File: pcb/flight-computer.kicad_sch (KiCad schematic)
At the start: 42 parts, among them J1 MicroSD Slot, J2 USB_C_Receptacle_USB2.0_16P, SW1 SW_Push, SW2 SW_Push, U1 RP2040, U2 W25Q16JVSS, U3 USBLC6-2SC6, Y1 12MHz

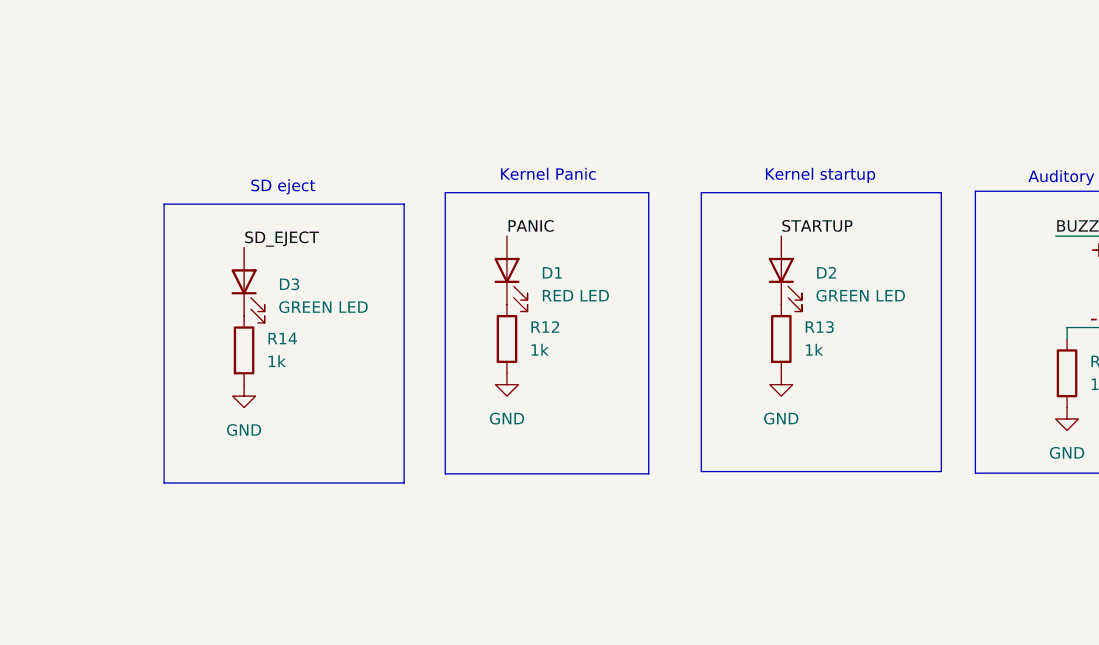
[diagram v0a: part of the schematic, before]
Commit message: Filled out the BOM for the schematic. Consolidated some components and changed footprint sizes.
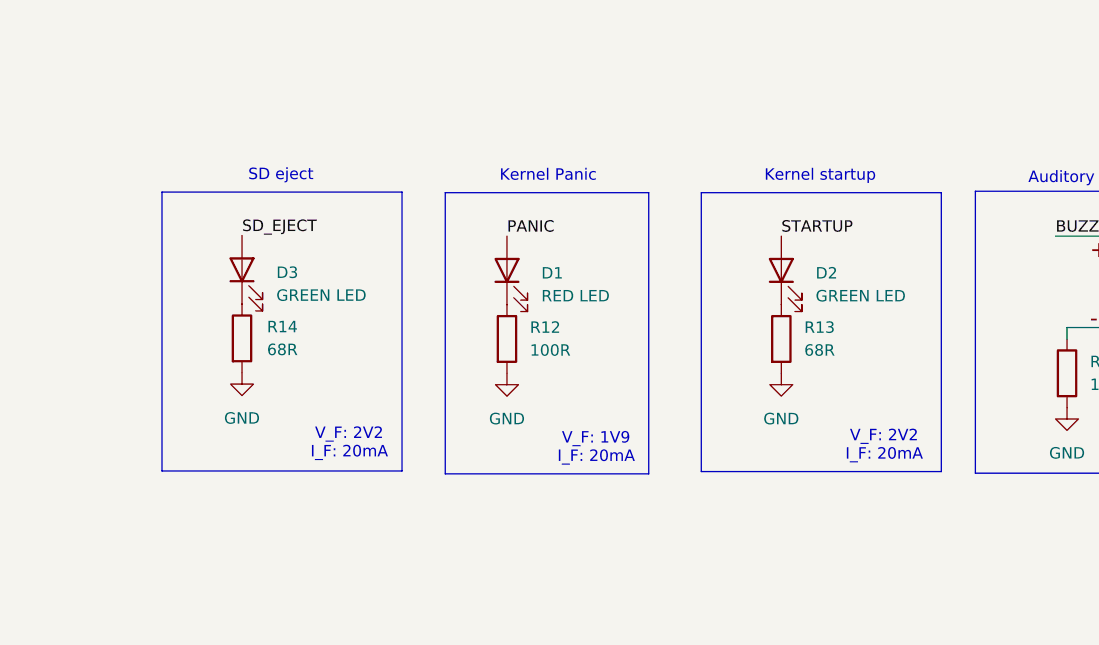
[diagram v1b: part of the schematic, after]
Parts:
- C1, C2: MP (none) -> 04023U140GAT2A
- C10, C11, C12, C13, C14, C15, C3, C5, C6, C8, C9: footprint Capacitor_SMD:C_0201_0603Metric -> Capacitor_SMD:C_0402_1005Metric; MP (none) -> GRM155R61A104KA01J
- C4: MP (none) -> GRM155C80J225KE95J
- C7: MP (none) -> 06036C105MAT2A
- D1: MP (none) -> HSMC-C170-T0000
- D2, D3: MP (none) -> LG R971-KN-1
- J1: MP (none) -> MEM2067-02-180-00-A
- J2: MP (none) -> USB4215-03-A
- LS1: MP (none) -> AI-1223-TWT-3V-2-R
- R1: footprint Resistor_SMD:R_0201_0603Metric -> Resistor_SMD:R_0402_1005Metric; MP (none) -> ERA-2AEB113X
- R10, R11: footprint Resistor_SMD:R_0201_0603Metric -> Resistor_SMD:R_0402_1005Metric; MP (none) -> MCS04020C5101FE000
- R12: value 1k -> 100R; footprint Resistor_SMD:R_0201_0603Metric -> Resistor_SMD:R_0402_1005Metric; MP (none) -> ERJ-U02J101X
- R13, R14: value 1k -> 68R; footprint Resistor_SMD:R_0201_0603Metric -> Resistor_SMD:R_0402_1005Metric; MP (none) -> ERA-2AED680X
- R15: footprint Resistor_SMD:R_0201_0603Metric -> Resistor_SMD:R_0402_1005Metric; MP (none) -> ERA-2AED151X
- R2, R9: footprint Resistor_SMD:R_0201_0603Metric -> Resistor_SMD:R_0402_1005Metric; MP (none) -> ERA-2AEB102X
- R3, R4, R5, R6: footprint Resistor_SMD:R_0201_0603Metric -> Resistor_SMD:R_0402_1005Metric; MP (none) -> ERA-2AEB222X
- R7, R8: footprint Resistor_SMD:R_0603_1608Metric -> Resistor_SMD:R_0402_1005Metric; MP (none) -> ERA-2AKD270X
- SW1, SW2: MP (none) -> TS02-66-50-BK-160-SCR-D
- U1: MP (none) -> SC0914(13)
- U2: MP (none) -> W25Q16JVSSIQ
- U3: MP (none) -> USBLC6-2SC6
- Y1: MP (none) -> ABM8-272-T3
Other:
- note added: "V_F: 1V9 I_F: 20mA"
- note added: "V_F: 2V2 I_F: 20mA"
- moved on the sheet: D3, R14

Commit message: Updated GPS to L86G
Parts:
- SW2: footprint Button_Switch_THT:SW_PUSH_6mm_H5mm -> Jumper:SolderJumper-2_P1.3mm_Open_TrianglePad1.0x1.5mm; MP TS02-66-50-BK-160-SCR-D -> (none)
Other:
- note removed: "Pullup sized for GPS"
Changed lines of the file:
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@@
 		)
 	)
-	(text "Pullup sized for GPS"
-		(exclude_from_sim no)
-		(at 104.394 48.006 0)
-		(effects
-			(font
-				(size 1.27 1.27)
-			)
-		)
-	)
 	(text "Auditory arming indicator"
 		(exclude_from_sim no)
@@
 			)
 		)
-		(property "Footprint" "Button_Switch_THT:SW_PUSH_6mm_H5mm"
+		(property "Footprint" "Jumper:SolderJumper-2_P1.3mm_Open_TrianglePad1.0x1.5mm"
 			(at 86.36 36.83 0)
 			(effects
@@
 			)
 		)
-		(property "Datasheet" "https://www.mouser.ca/datasheet/2/1628/ts02-3511329.pdf"
+		(property "Datasheet" ""
 			(at 86.36 36.83 0)
 			(effects
@@
 			)
 		)
-		(property "MP" "TS02-66-50-BK-160-SCR-D"
+		(property "MP" ""
 			(at 86.36 41.91 0)
 			(effects

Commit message: Added mounting holes and copper pours.
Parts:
- added H1, H2, H3, H4: MountingHole, MountingHole:MountingHole_3.2mm_M3, symbol Mechanical:MountingHole
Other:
- note added: "M3 mounting holes"

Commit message: Almost done routing
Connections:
- net RD-: now reaches R8.2, U1.46 (USB_DM)
- net RD+: now reaches R7.2, U1.47 (USB_DP)
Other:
- moved on the sheet: R7, R8
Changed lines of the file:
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@@
 	(wire
 		(pts
-			(xy 168.91 60.96) (xy 171.45 60.96)
+			(xy 165.1 60.96) (xy 171.45 60.96)
 		)
 		(stroke
@@
 	(wire
 		(pts
-			(xy 147.32 63.5) (xy 154.94 63.5)
+			(xy 143.51 63.5) (xy 151.13 63.5)
 		)
 		(stroke
@@
 	(wire
 		(pts
-			(xy 147.32 60.96) (xy 161.29 60.96)
+			(xy 143.51 60.96) (xy 157.48 60.96)
 		)
 		(stroke
@@
 	(wire
 		(pts
-			(xy 162.56 63.5) (xy 171.45 63.5)
+			(xy 158.75 63.5) (xy 171.45 63.5)
 		)
 		(stroke
@@
 		)
 	)
+	(label "RD+"
+		(at 166.37 60.96 0)
+		(fields_autoplaced yes)
+		(effects
+			(font
+				(size 1.27 1.27)
+			)
+			(justify left bottom)
+		)
+	)
 	(label "SPI1_CS"
 		(at 34.29 237.49 0)
@@
 		)
 	)
+	(label "RD-"
+		(at 166.37 63.5 0)
+		(fields_autoplaced yes)
+		(effects
+			(font
+				(size 1.27 1.27)
+			)
+			(justify left bottom)
+		)
+	)
 	(label "MCU_D-"
 		(at 166.37 247.65 0)
@@
 	)
 	(label "MCU_D-"
-		(at 147.32 63.5 0)
+		(at 143.51 63.5 0)
 		(fields_autoplaced yes)
 		(effects
@@
 	)
 	(label "MCU_D+"
-		(at 147.32 60.96 0)
+		(at 143.51 60.96 0)
 		(fields_autoplaced yes)
 		(effects
@@
 	(symbol
 		(lib_id "Device:R")
-		(at 158.75 63.5 90)
+		(at 154.94 63.5 90)
 		(unit 1)
 		(exclude_from_sim no)
@@
 		(fields_autoplaced yes)
 		(property "Reference" "R8"
-			(at 158.75 57.15 90)
+			(at 154.94 57.15 90)
 			(effects
 				(font
@@
 		)
 		(property "Value" "27R"
-			(at 158.75 59.69 90)
+			(at 154.94 59.69 90)
 			(effects
 				(font
@@
 		)
 		(property "Footprint" "Resistor_SMD:R_0402_1005Metric"
-			(at 158.75 65.278 90)
+			(at 154.94 65.278 90)
 			(effects
 				(font
@@
 		)
 		(property "Datasheet" "https://www.mouser.ca/datasheet/2/315/AOA0000C307-1149632.pdf"
-			(at 158.75 63.5 0)
+			(at 154.94 63.5 0)
 			(effects
 				(font
@@
 		)
 		(property "Description" "Resistor"
-			(at 158.75 63.5 0)
+			(at 154.94 63.5 0)
 			(effects
 				(font
@@
 		)
 		(property "MP" "ERA-2AKD270X"
-			(at 158.75 63.5 0)
+			(at 154.94 63.5 0)
 			(effects
 				(font
@@
 	(symbol
 		(lib_id "Device:R")
-		(at 165.1 60.96 90)
+		(at 161.29 60.96 90)
 		(unit 1)
 		(exclude_from_sim no)
@@
 		(fields_autoplaced yes)
 		(property "Reference" "R7"
-			(at 165.1 54.61 90)
+			(at 161.29 54.61 90)
 			(effects
 				(font
@@
 		)
 		(property "Value" "27R"
-			(at 165.1 57.15 90)
+			(at 161.29 57.15 90)
 			(effects
 				(font
@@
 		)
 		(property "Footprint" "Resistor_SMD:R_0402_1005Metric"
-			(at 165.1 62.738 90)
+			(at 161.29 62.738 90)
 			(effects
 				(font
@@
 		)
 		(property "Datasheet" "https://www.mouser.ca/datasheet/2/315/AOA0000C307-1149632.pdf"
-			(at 165.1 60.96 0)
+			(at 161.29 60.96 0)
 			(effects
 				(font
@@
 		)
 		(property "Description" "Resistor"
-			(at 165.1 60.96 0)
+			(at 161.29 60.96 0)
 			(effects
 				(font
@@
 		)
 		(property "MP" "ERA-2AKD270X"
-			(at 165.1 60.96 0)
+			(at 161.29 60.96 0)
 			(effects
 				(font
